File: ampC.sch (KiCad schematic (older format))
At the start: 13 parts, among them U19 Mux, U6 TL084, U8 screw_term, U9 screw_term

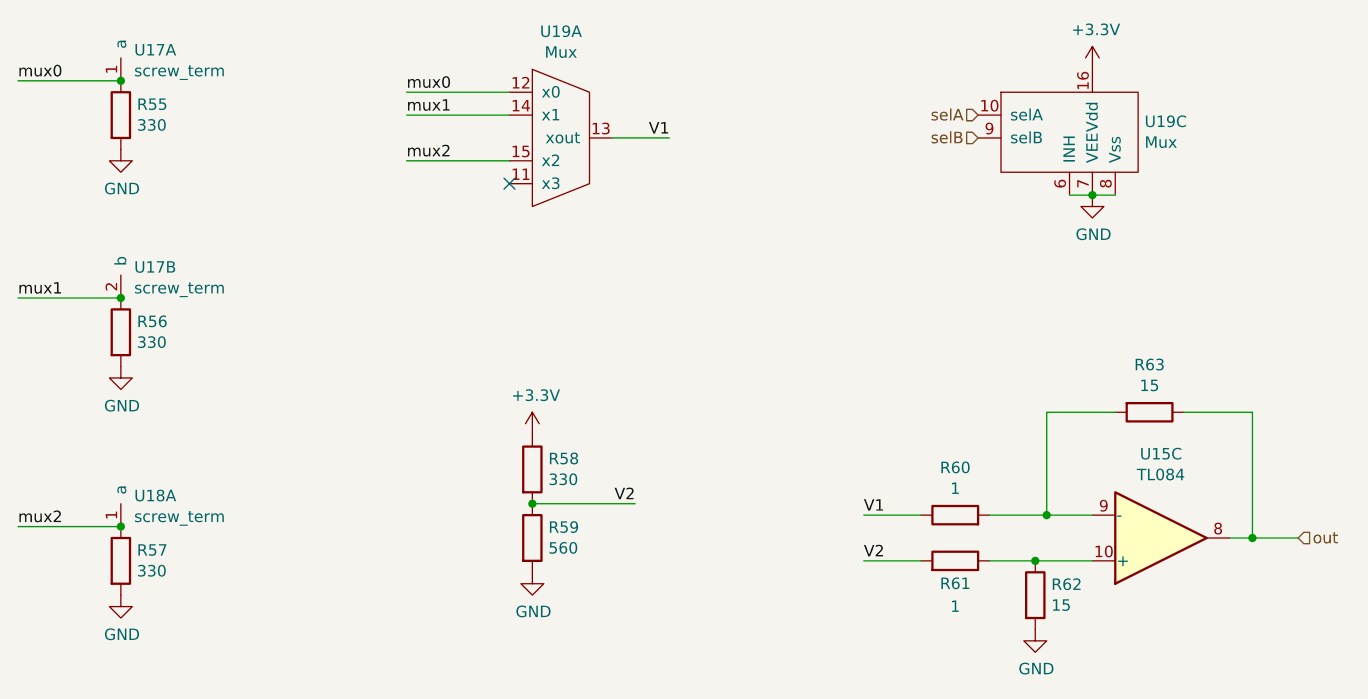
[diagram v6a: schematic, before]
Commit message: changed to mcp6004 op amp
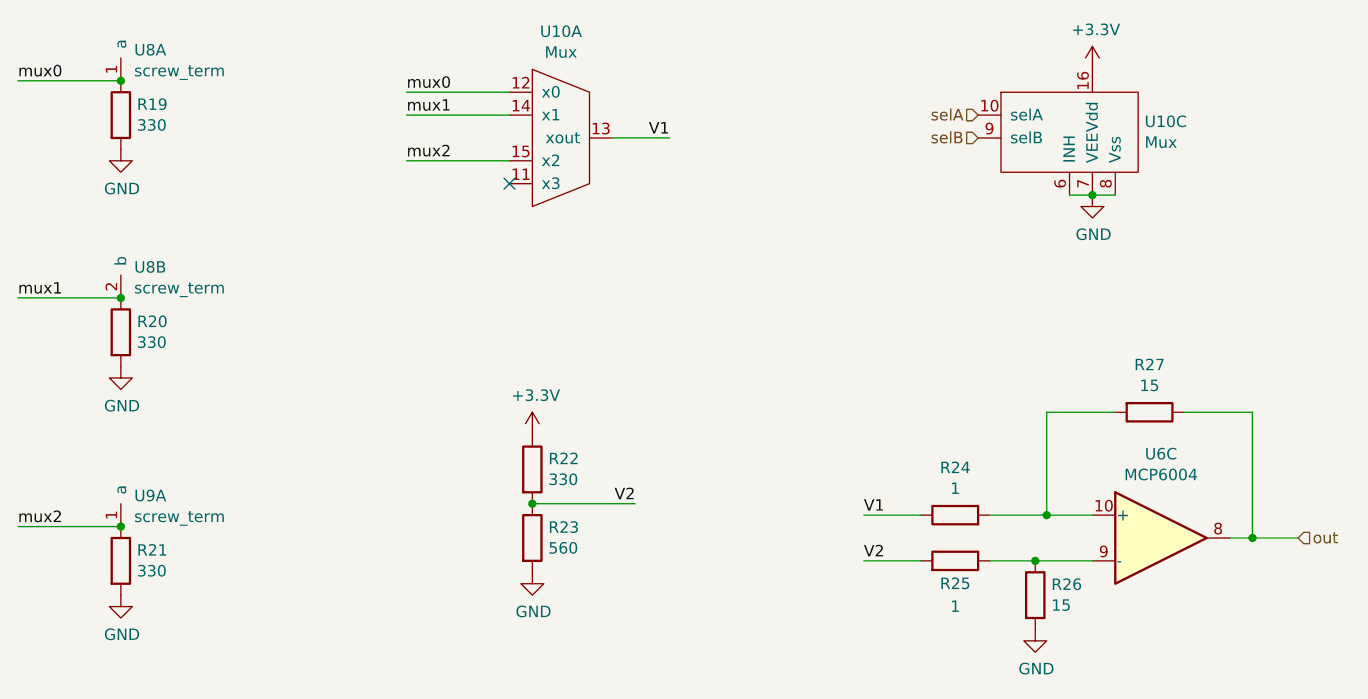
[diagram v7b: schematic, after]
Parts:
- removed U6: TL084, Package_DIP:DIP-14_W7.62mm, symbol Amplifier_Operational:TL084
- added U6: MCP6004, Package_DIP:DIP-14_W7.62mm, symbol Amplifier_Operational:MCP6004
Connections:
- net out: now also U6.8
- net at R25.1, R26.1: now also U6.9 (-)
- net at R24.2, R27.2: now also U6.10 (+)
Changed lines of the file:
@@
 $Descr A4 11693 8268
 encoding utf-8
-Sheet 8 11
+Sheet 4 11
 Title ""
 Date ""
@@
 AR Path="/6019C043/6019D554" Ref="#PWR024"  Part="1"
 AR Path="/601B4C16/6019D554" Ref="#PWR054"  Part="1"
-F 0 "#PWR054" H 1450 1850 50  0001 C CNN
+F 0 "#PWR024" H 1450 1850 50  0001 C CNN
 F 1 "GND" H 1455 1927 50  0000 C CNN
 F 2 "" H 1450 2100 50  0001 C CNN
@@
 	1    1450 2100
 	1    0    0    -1
-$EndComp
-$Comp
-L Amplifier_Operational:TL084 U?
-U 3 1 6019D566
-P 6000 3800
-AR Path="/60132BC3/6013AE22/6019D566" Ref="U?"  Part="1"
-AR Path="/6017CC5E/6019D566" Ref="U?"  Part="1"
-AR Path="/6017DA21/6019D566" Ref="U?"  Part="1"
-AR Path="/601927EB/6019D566" Ref="U?"  Part="1"
-AR Path="/6019C043/6019D566" Ref="U6"  Part="3"
-AR Path="/601B4C16/6019D566" Ref="U15"  Part="3"
-F 0 "U15" H 6000 3433 50  0000 C CNN
-F 1 "TL084" H 6000 3524 50  0000 C CNN
-F 2 "Package_DIP:DIP-14_W7.62mm" H 5950 3900 50  0001 C CNN
-F 3 "http://www.ti.com/lit/ds/symlink/tl081.pdf" H 6050 4000 50  0001 C CNN
-	3    6000 3800
-	1    0    0    1
 $EndComp
 $Comp
@@
 AR Path="/6019C043/60198F28" Ref="R26"  Part="1"
 AR Path="/601B4C16/60198F28" Ref="R62"  Part="1"
-F 0 "R62" H 5520 4096 50  0000 L CNN
+F 0 "R26" H 5520 4096 50  0000 L CNN
 F 1 "15" H 5520 4005 50  0000 L CNN
 F 2 "Resistor_THT:R_Axial_DIN0204_L3.6mm_D1.6mm_P5.08mm_Horizontal" V 5380 4050 50  0001 C CNN
@@
 AR Path="/6019C043/6019D567" Ref="R27"  Part="1"
 AR Path="/601B4C16/6019D567" Ref="R63"  Part="1"
-F 0 "R63" V 5743 3250 50  0000 C CNN
+F 0 "R27" V 5743 3250 50  0000 C CNN
 F 1 "15" V 5834 3250 50  0000 C CNN
 F 2 "Resistor_THT:R_Axial_DIN0204_L3.6mm_D1.6mm_P5.08mm_Horizontal" V 5880 3250 50  0001 C CNN
@@
 AR Path="/6019C043/6019D55D" Ref="R24"  Part="1"
 AR Path="/601B4C16/6019D55D" Ref="R60"  Part="1"
-F 0 "R60" V 5307 3700 50  0000 C CNN
+F 0 "R24" V 5307 3700 50  0000 C CNN
 F 1 "1" V 5216 3700 50  0000 C CNN
 F 2 "Resistor_THT:R_Axial_DIN0204_L3.6mm_D1.6mm_P5.08mm_Horizontal" V 5030 3700 50  0001 C CNN
@@
 AR Path="/6019C043/60198F34" Ref="R25"  Part="1"
 AR Path="/601B4C16/60198F34" Ref="R61"  Part="1"
-F 0 "R61" V 5000 3900 50  0000 C CNN
+F 0 "R25" V 5000 3900 50  0000 C CNN
 F 1 "1" V 4900 3900 50  0000 C CNN
 F 2 "Resistor_THT:R_Axial_DIN0204_L3.6mm_D1.6mm_P5.08mm_Horizontal" V 5030 3900 50  0001 C CNN
@@
 AR Path="/6019C043/6017E433" Ref="R22"  Part="1"
 AR Path="/601B4C16/6017E433" Ref="R58"  Part="1"
-F 0 "R58" H 3320 3546 50  0000 L CNN
+F 0 "R22" H 3320 3546 50  0000 L CNN
 F 1 "330" H 3320 3455 50  0000 L CNN
 F 2 "Resistor_THT:R_Axial_DIN0204_L3.6mm_D1.6mm_P5.08mm_Horizontal" V 3180 3500 50  0001 C CNN
@@
 AR Path="/6019C043/6017E434" Ref="R23"  Part="1"
 AR Path="/601B4C16/6017E434" Ref="R59"  Part="1"
-F 0 "R59" H 3320 3846 50  0000 L CNN
+F 0 "R23" H 3320 3846 50  0000 L CNN
 F 1 "560" H 3320 3755 50  0000 L CNN
 F 2 "Resistor_THT:R_Axial_DIN0204_L3.6mm_D1.6mm_P5.08mm_Horizontal" V 3180 3800 50  0001 C CNN
@@
 AR Path="/6019C043/6017E435" Ref="#PWR027"  Part="1"
 AR Path="/601B4C16/6017E435" Ref="#PWR057"  Part="1"
-F 0 "#PWR057" H 3250 3200 50  0001 C CNN
+F 0 "#PWR027" H 3250 3200 50  0001 C CNN
 F 1 "+3.3V" H 3265 3523 50  0000 C CNN
 F 2 "" H 3250 3350 50  0001 C CNN
@@
 AR Path="/6019C043/6019D569" Ref="#PWR028"  Part="1"
 AR Path="/601B4C16/6019D569" Ref="#PWR058"  Part="1"
-F 0 "#PWR058" H 3250 3700 50  0001 C CNN
+F 0 "#PWR028" H 3250 3700 50  0001 C CNN
 F 1 "GND" H 3255 3777 50  0000 C CNN
 F 2 "" H 3250 3950 50  0001 C CNN
@@
 AR Path="/6019C043/6019D555" Ref="#PWR029"  Part="1"
 AR Path="/601B4C16/6019D555" Ref="#PWR059"  Part="1"
-F 0 "#PWR059" H 5450 3950 50  0001 C CNN
+F 0 "#PWR029" H 5450 3950 50  0001 C CNN
 F 1 "GND" H 5455 4027 50  0000 C CNN
 F 2 "" H 5450 4200 50  0001 C CNN
@@
 AR Path="/6019C043/6019D556" Ref="R19"  Part="1"
 AR Path="/601B4C16/6019D556" Ref="R55"  Part="1"
-F 0 "R55" H 1520 1996 50  0000 L CNN
+F 0 "R19" H 1520 1996 50  0000 L CNN
 F 1 "330" H 1520 1905 50  0000 L CNN
 F 2 "Resistor_THT:R_Axial_DIN0204_L3.6mm_D1.6mm_P5.08mm_Horizontal" V 1380 1950 50  0001 C CNN
@@
 AR Path="/6019C043/6019D557" Ref="U8"  Part="1"
 AR Path="/601B4C16/6019D557" Ref="U17"  Part="1"
-F 0 "U17" H 1508 1934 50  0000 L CNN
+F 0 "U8" H 1508 1934 50  0000 L CNN
 F 1 "screw_term" H 1508 1843 50  0000 L CNN
 F 2 "Connector_PinHeader_1.27mm:PinHeader_1x02_P1.27mm_Vertical" H 1450 1800 50  0001 C CNN
@@
 AR Path="/6019C043/60176F19" Ref="#PWR025"  Part="1"
 AR Path="/601B4C16/60176F19" Ref="#PWR055"  Part="1"
-F 0 "#PWR055" H 1450 2800 50  0001 C CNN
+F 0 "#PWR025" H 1450 2800 50  0001 C CNN
 F 1 "GND" H 1455 2877 50  0000 C CNN
 F 2 "" H 1450 3050 50  0001 C CNN
@@
 AR Path="/6019C043/60198F39" Ref="R20"  Part="1"
 AR Path="/601B4C16/60198F39" Ref="R56"  Part="1"
-F 0 "R56" H 1520 2946 50  0000 L CNN
+F 0 "R20" H 1520 2946 50  0000 L CNN
 F 1 "330" H 1520 2855 50  0000 L CNN
 F 2 "Resistor_THT:R_Axial_DIN0204_L3.6mm_D1.6mm_P5.08mm_Horizontal" V 1380 2900 50  0001 C CNN
@@
 AR Path="/6019C043/6019D55A" Ref="U8"  Part="2"
 AR Path="/601B4C16/6019D55A" Ref="U17"  Part="2"
-F 0 "U17" H 1508 2884 50  0000 L CNN
+F 0 "U8" H 1508 2884 50  0000 L CNN
 F 1 "screw_term" H 1508 2793 50  0000 L CNN
 F 2 "Connector_PinHeader_1.27mm:PinHeader_1x02_P1.27mm_Vertical" H 1450 2750 50  0001 C CNN
@@
 AR Path="/6019C043/60177983" Ref="#PWR026"  Part="1"
 AR Path="/601B4C16/60177983" Ref="#PWR056"  Part="1"
-F 0 "#PWR056" H 1450 3800 50  0001 C CNN
+F 0 "#PWR026" H 1450 3800 50  0001 C CNN
 F 1 "GND" H 1455 3877 50  0000 C CNN
 F 2 "" H 1450 4050 50  0001 C CNN
@@
 AR Path="/6019C043/6019D561" Ref="R21"  Part="1"
 AR Path="/601B4C16/6019D561" Ref="R57"  Part="1"
-F 0 "R57" H 1520 3946 50  0000 L CNN
+F 0 "R21" H 1520 3946 50  0000 L CNN
 F 1 "330" H 1520 3855 50  0000 L CNN
 F 2 "Resistor_THT:R_Axial_DIN0204_L3.6mm_D1.6mm_P5.08mm_Horizontal" V 1380 3900 50  0001 C CNN
@@
 AR Path="/6019C043/6017798F" Ref="U9"  Part="1"
 AR Path="/601B4C16/6017798F" Ref="U18"  Part="1"
-F 0 "U18" H 1508 3884 50  0000 L CNN
+F 0 "U9" H 1508 3884 50  0000 L CNN
 F 1 "screw_term" H 1508 3793 50  0000 L CNN
 F 2 "Connector_PinHeader_1.27mm:PinHeader_1x02_P1.27mm_Vertical" H 1450 3750 50  0001 C CNN
@@
 AR Path="/6019C043/6019D563" Ref="#PWR031"  Part="1"
 AR Path="/601B4C16/6019D563" Ref="#PWR061"  Part="1"
-F 0 "#PWR061" H 5700 2050 50  0001 C CNN
+F 0 "#PWR031" H 5700 2050 50  0001 C CNN
 F 1 "GND" H 5705 2127 50  0000 C CNN
 F 2 "" H 5700 2300 50  0001 C CNN
@@
 AR Path="/6019C043/6019D564" Ref="#PWR030"  Part="1"
 AR Path="/601B4C16/6019D564" Ref="#PWR060"  Part="1"
-F 0 "#PWR060" H 5700 1600 50  0001 C CNN
+F 0 "#PWR030" H 5700 1600 50  0001 C CNN
 F 1 "+3.3V" H 5715 1923 50  0000 C CNN
 F 2 "" H 5700 1750 50  0001 C CNN
@@
 AR Path="/601B4C16/601763C1" Ref="U19"  Part="1"
 AR Path="/6019C043/601763C1" Ref="U10"  Part="1"
-F 0 "U19" H 3375 2515 50  0000 C CNN
+F 0 "U10" H 3375 2515 50  0000 C CNN
 F 1 "Mux" H 3375 2424 50  0000 C CNN
 F 2 "Package_DIP:DIP-16_W7.62mm" H 3350 2050 50  0001 C CNN
@@
 AR Path="/601B4C16/60176BAF" Ref="U19"  Part="3"
 AR Path="/6019C043/60176BAF" Ref="U10"  Part="3"
-F 0 "U19" H 5928 2221 50  0000 L CNN
+F 0 "U10" H 5928 2221 50  0000 L CNN
 F 1 "Mux" H 5928 2130 50  0000 L CNN
 F 2 "Package_DIP:DIP-16_W7.62mm" H 5700 2100 50  0001 C CNN
@@
 	1    0    0    -1
 $EndComp
+$Comp
+L Amplifier_Operational:MCP6004 U6
+U 3 1 6018DE62
+P 6000 3800
+AR Path="/6019C043/6018DE62" Ref="U6"  Part="3"
+AR Path="/601B4C16/6018DE62" Ref="U15"  Part="3"
+F 0 "U6" H 6000 4167 50  0000 C CNN
+F 1 "MCP6004" H 6000 4076 50  0000 C CNN
+F 2 "Package_DIP:DIP-14_W7.62mm" H 5950 3900 50  0001 C CNN
+F 3 "http://ww1.microchip.com/downloads/en/DeviceDoc/21733j.pdf" H 6050 4000 50  0001 C CNN
+	3    6000 3800
+	1    0    0    -1
+$EndComp
